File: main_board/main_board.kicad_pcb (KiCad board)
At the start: 4 copper layers, 85 x 55 mm, 45 parts, among them J1 USB_B_Micro, J2 Conn_ARM_JTAG_SWD_10, Q2 T2N7002AK,LM, U1 SSD1306, U2 ESP32-S2-SOLO, U3 TLV62568PDRLT, U4 MCP73832, Y1 SC32S-7PF20PPM

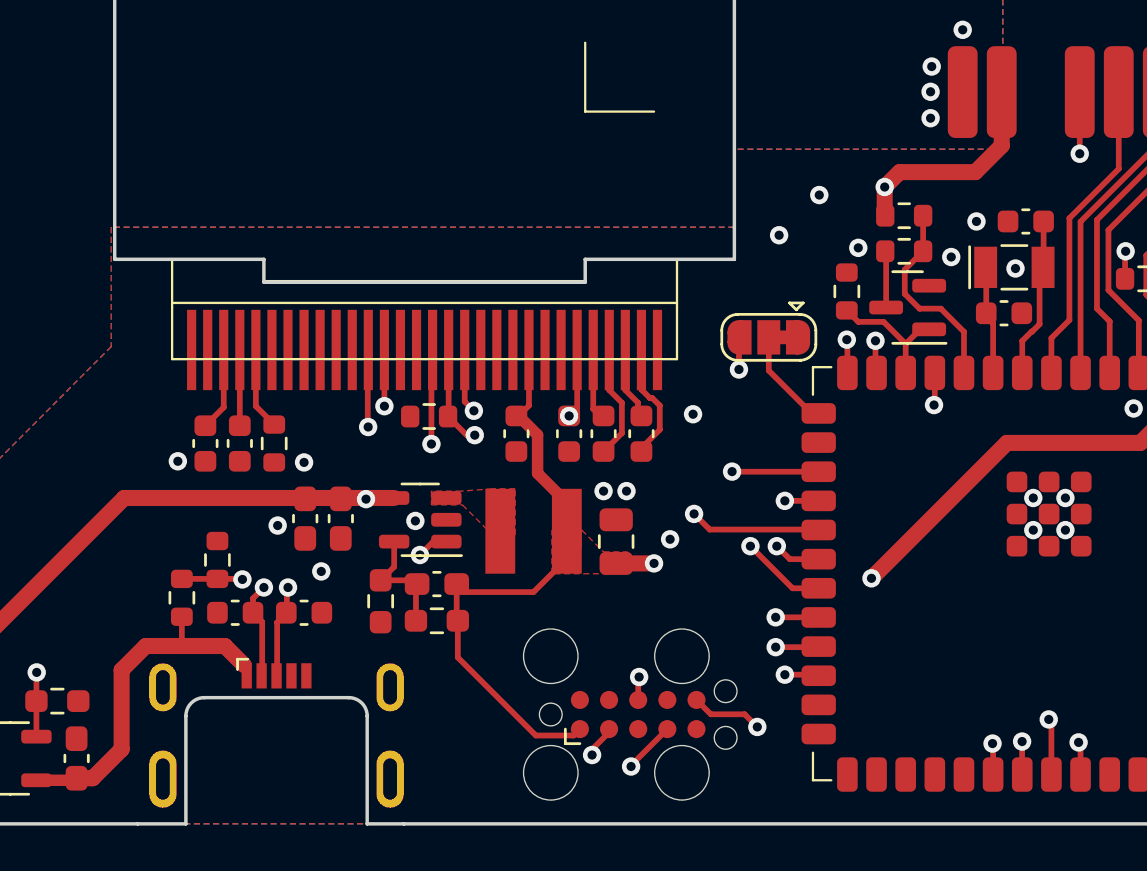
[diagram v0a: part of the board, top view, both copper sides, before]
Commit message: Fix #12: add PFET
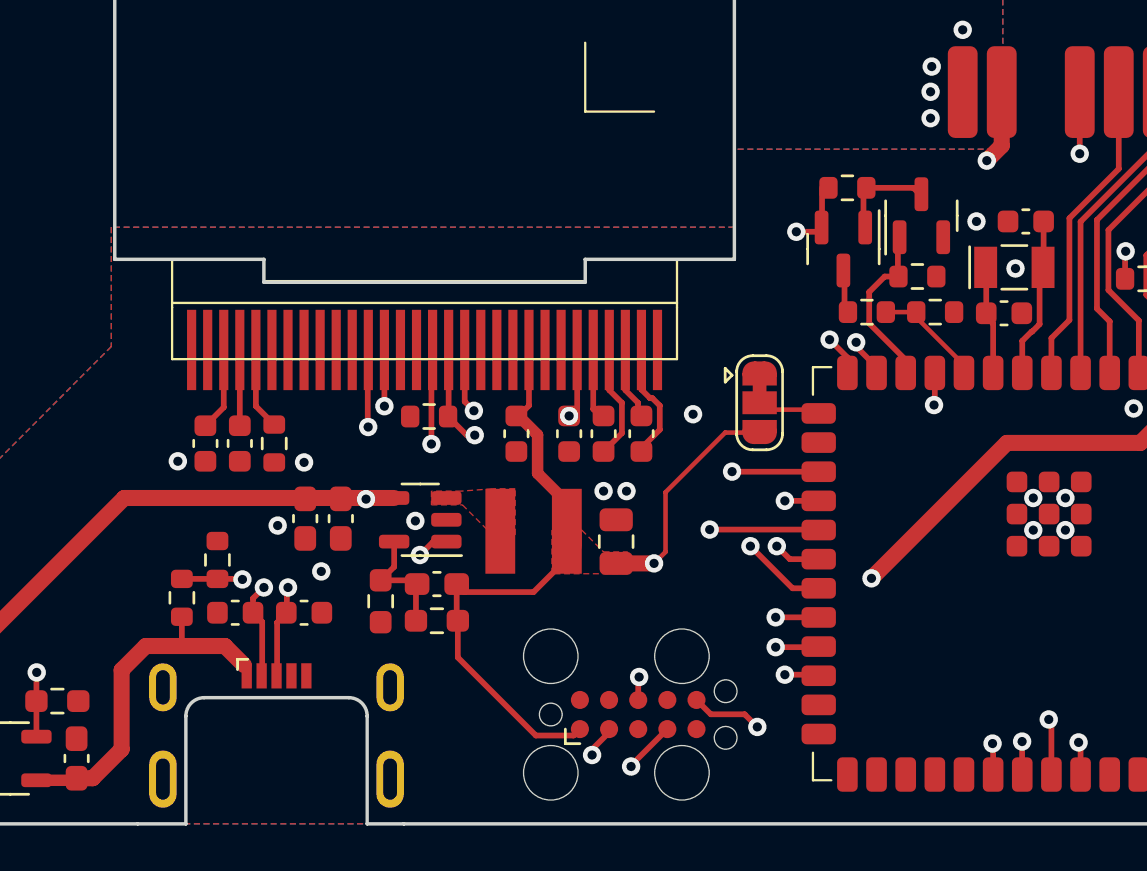
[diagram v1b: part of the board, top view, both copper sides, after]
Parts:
- added Q1: NX3008PBK,215, Package_TO_SOT_SMD:SOT-23, F.Cu at (140.8, 75.0)
- added R13: 1M, Resistor_SMD:R_0603_1608Metric, F.Cu at (140.9, 72.3)
- moved R12 4.50 mm to (141.8, 77.7)
- moved Q2 4.04 mm to (144.2, 73.5), turned to 90 degrees
- moved R9 3.14 mm to (144.0, 76.2), turned to 0 degrees
- moved R11 2.97 mm to (144.8, 77.7), turned to 0 degrees
- moved JP1 2.88 mm to (137.1, 81.7), turned to -90 degrees
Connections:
- Q2 pad 3: Net-(Q2-D) -> Net-(Q1-G)
- R11 pad 2: Net-(Q2-D) -> GND
- R12 pad 1: +BATT -> Net-(Q1-D)
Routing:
- net +3V3: track 85.4 -> 81.0 mm, vias 3 -> 2
- net Net-(Q1-G): track 0.00 -> 4.26 mm
- net /BATT_ADC: track 8.75 -> 4.84 mm
- net +BATT: track 79.9 -> 82.4 mm, vias 4 -> 5
- net Net-(Q2-D): track 2.47 -> 0.00 mm
- net Net-(Q1-D): track 0.00 -> 1.93 mm
- net /ADC_EN: track 5.72 -> 7.46 mm
- net Net-(JP1-C): track 4.40 -> 2.77 mm
- net /USB_D-: track 37.3 -> 36.7 mm
- net GND: vias 32 -> 27

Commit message: Fix #18: add RLD output, fix main board revision
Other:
- board text added: "Card/IO v1r2 Not for medical use"
- board text removed: "Card/IO v1r1 Not for medical use"
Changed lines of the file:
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@@
     (effects (font (size 1 1) (thickness 0.2) bold) (justify left bottom mirror))
   )
-  (gr_text "Card/IO v1r1\nNot for medical use" (at 129.9 53.15) (layer "B.SilkS")
+  (gr_text "Card/IO v1r2\nNot for medical use" (at 129.9 53.15) (layer "B.SilkS")
     (effects (font (size 1 1) (thickness 0.15)) (justify left bottom mirror))
   )

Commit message: Add changes to layout
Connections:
- M1 pad 10: GND -> Net-(M1-~{DRDY})
- M1 pad 11: +3V3 -> GND
- M1 pad 12: /ECG_EN -> +3V3
- M1 pad 13: /~{TOUCH} -> /ECG_CLK_EN
- M1 pad 3: GNDA -> unconnected-(M1-RLD_OUT-Pad3)
- M1 pad 4: +BATT -> GNDA
- M1 pad 5: Net-(M1-~{CS}) -> +BATT
- M1 pad 6: Net-(M1-MOSI) -> Net-(M1-~{CS})
- M1 pad 7: Net-(M1-SCLK) -> Net-(M1-MOSI)
- M1 pad 8: Net-(M1-MISO) -> Net-(M1-SCLK)
- M1 pad 9: Net-(M1-~{DRDY}) -> Net-(M1-MISO)
- U2 pad 31: unconnected-(U2-IO38-Pad31) -> /ECG_CLK_EN
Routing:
- net /ECG_CLK_EN: track 0.00 -> 51.1 mm, vias 0 -> 2
- net /ECG_EN: track 43.6 -> 46.4 mm
- net Net-(J2-NC/TDI): track 22.8 -> 23.7 mm

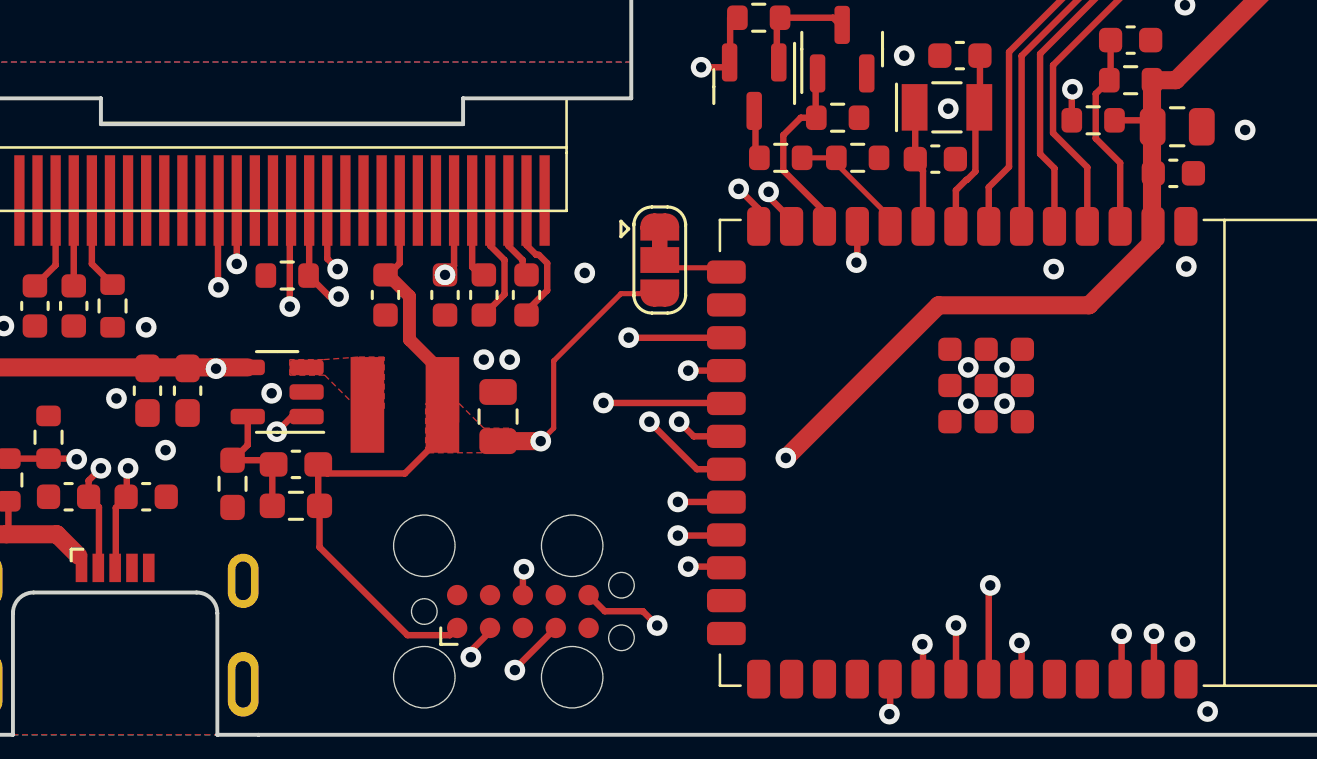
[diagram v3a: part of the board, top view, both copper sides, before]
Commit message: Fix #19: shuffle pin assignment
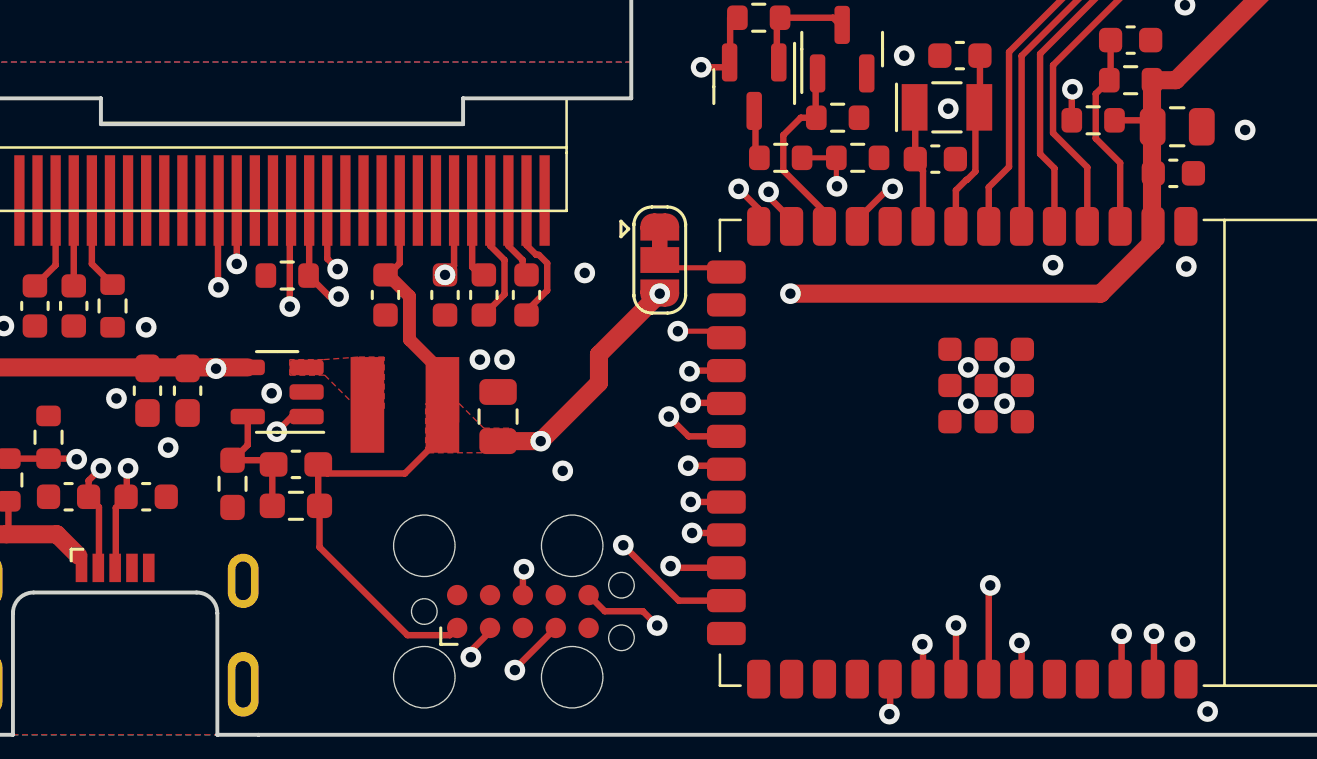
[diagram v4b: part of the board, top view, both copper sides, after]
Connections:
- U2 pad 10: /BATT_ADC -> unconnected-(U2-IO17-Pad10)
- U2 pad 17: /~{DISPLAY_RES} -> /BATT_ADC
- U2 pad 18: /~{DISPLAY_CS} -> /CHG_CURRENT
- U2 pad 19: /DISPLAY_MOSI -> /~{DISPLAY_CS}
- U2 pad 20: /DISPLAY_SCK -> /~{DISPLAY_RES}
- U2 pad 22: /CHG_CURRENT -> /DISPLAY_SCK
- U2 pad 23: /CHG_STAT -> /DISPLAY_MOSI
- U2 pad 24: /VBUS_DETECT -> /CHG_STAT
- U2 pad 25: unconnected-(U2-IO34-Pad25) -> /VBUS_DETECT
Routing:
- net +3V3: track 81.0 -> 72.6 mm, vias 2 -> 3
- net /BATT_ADC: track 4.84 -> 13.1 mm, vias 0 -> 2
- net /DISPLAY_MOSI: track 24.9 -> 27.4 mm
- net Net-(M1-~{CS}): track 21.5 -> 19.6 mm
- net /CHG_CURRENT: track 38.3 -> 40.0 mm, vias 2 -> 3
- net /DISPLAY_SCK: track 24.1 -> 25.7 mm
- net /~{DISPLAY_RES}: track 20.0 -> 21.5 mm
- net /VBUS_DETECT: track 29.9 -> 30.7 mm
- net /CHG_STAT: track 39.7 -> 40.3 mm
- net /~{DISPLAY_CS}: track 19.5 -> 20.0 mm

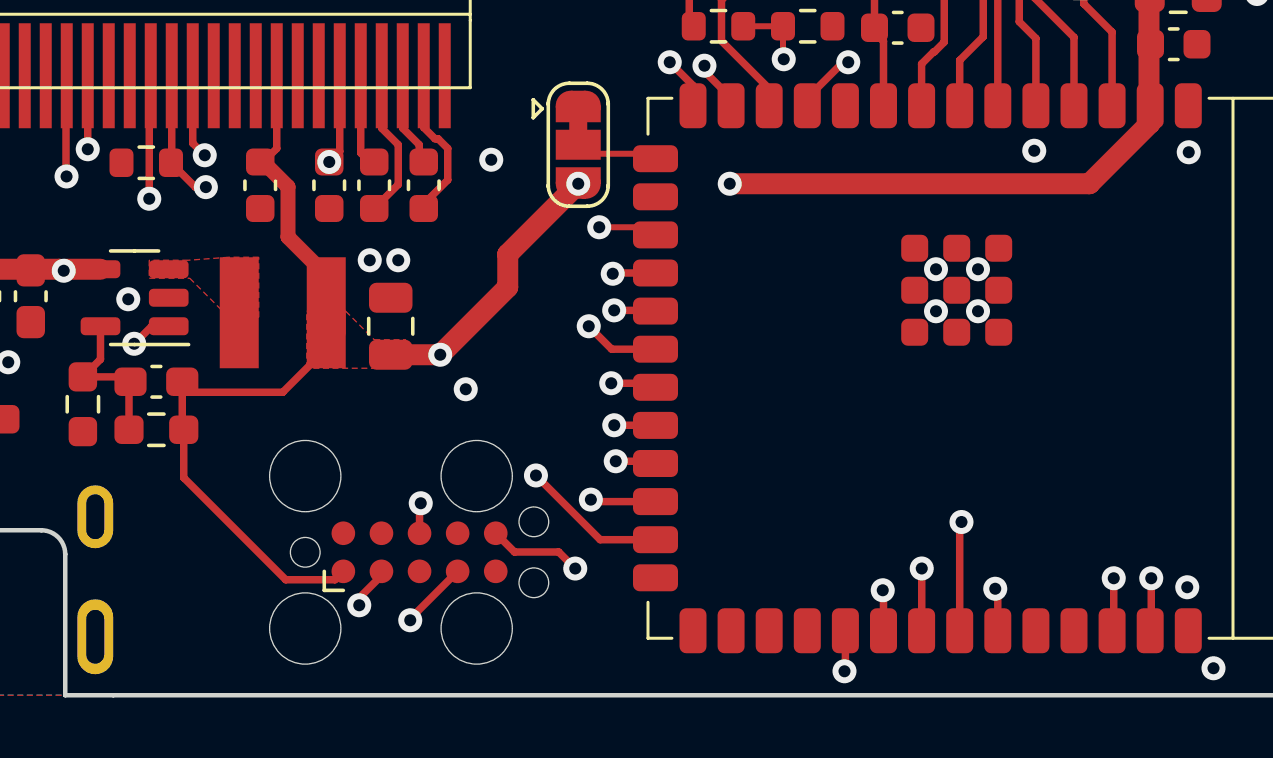
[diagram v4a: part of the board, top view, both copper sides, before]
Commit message: Fix #16: move JTAG to front side
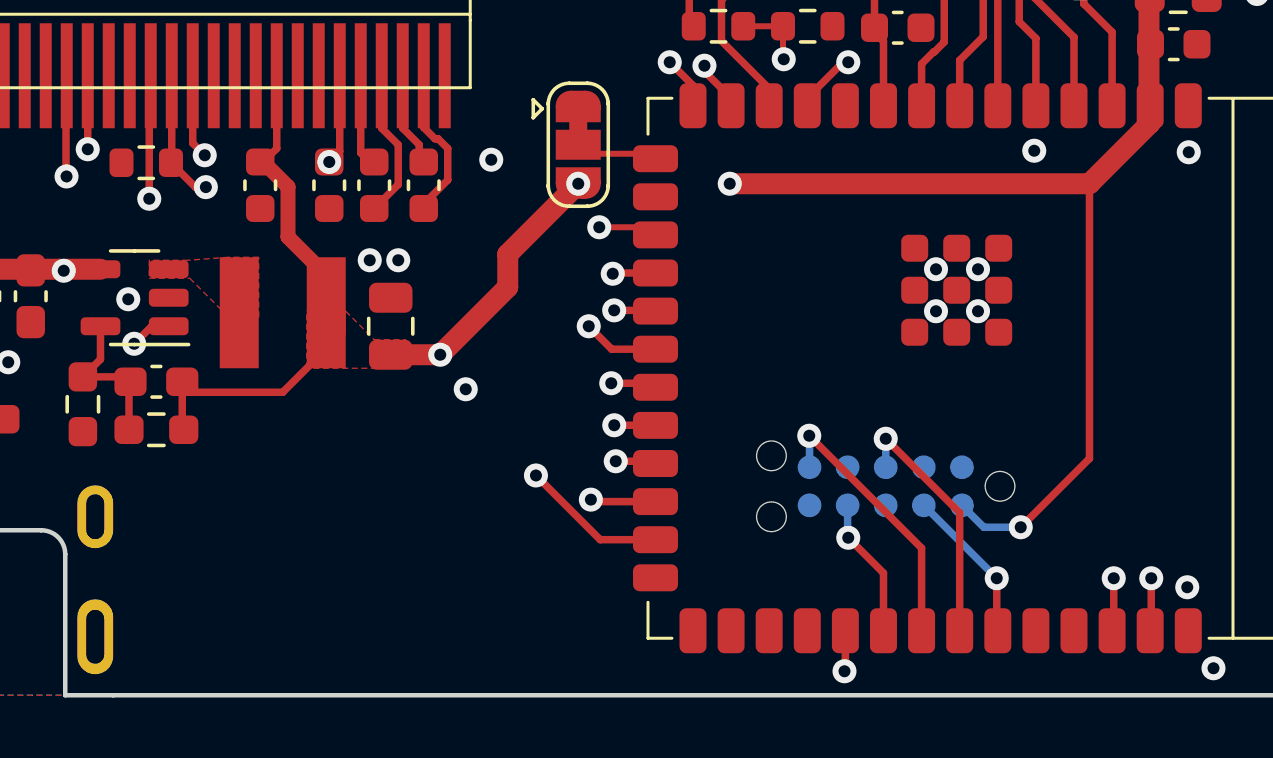
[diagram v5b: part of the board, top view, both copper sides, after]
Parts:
- J2: footprint Connector:Tag-Connect_TC2050-IDC-FP_2x05_P1.27mm_Vertical -> Connector:Tag-Connect_TC2050-IDC-NL_2x05_P1.27mm_Vertical; moved to B.Cu
- moved J2 15.7 mm to (147.3, 93.0), turned to 180 degrees
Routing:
- net Net-(J2-SWDIO/TMS): track 25.5 -> 5.20 mm, vias 2 -> 1
- net Net-(J2-SWDCLK/TCK): track 20.6 -> 4.67 mm, vias 2 -> 1
- net Net-(J2-NC/TDI): track 23.7 -> 8.37 mm, vias 2 -> 1
- net Net-(J2-SWO/TDO): track 16.8 -> 9.11 mm, vias 2 -> 1
- net +3V3: track 72.6 -> 78.8 mm, vias 3 -> 4

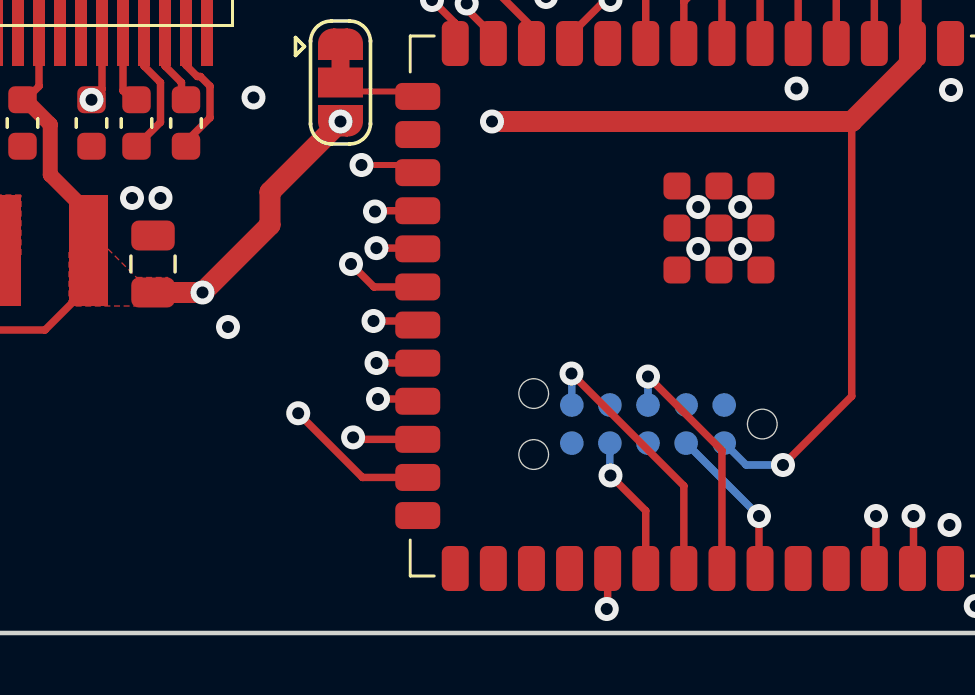
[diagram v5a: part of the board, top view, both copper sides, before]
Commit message: Tweak routing a bit
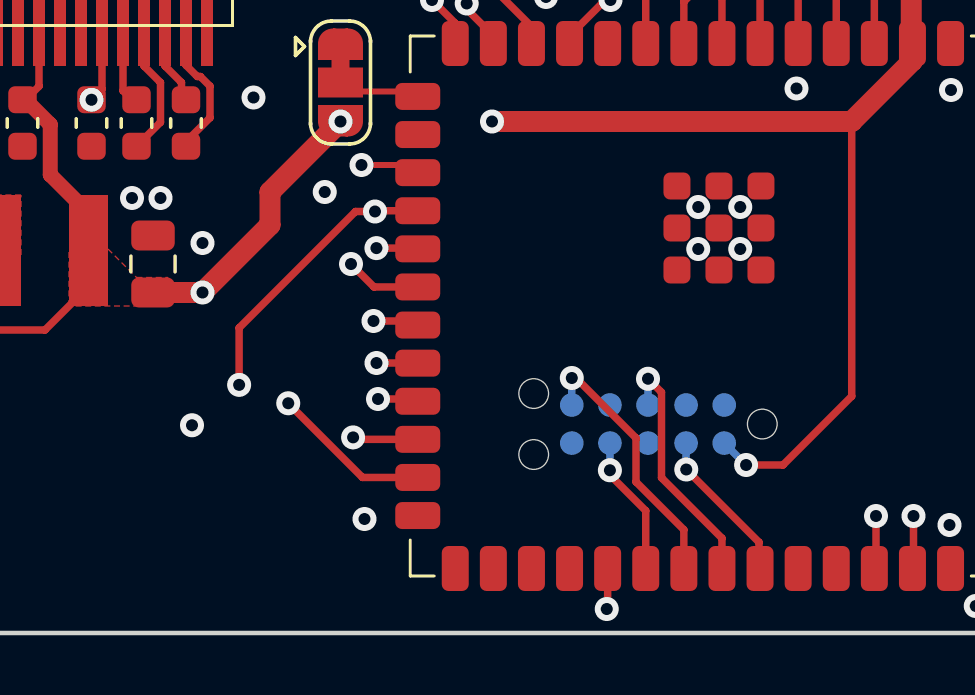
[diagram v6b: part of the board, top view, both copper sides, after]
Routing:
- net /BATT_ADC: track 13.1 -> 15.6 mm
- net /CHG_CURRENT: track 40.0 -> 41.3 mm
- net /CHG_STAT: track 40.3 -> 39.5 mm
- net GND: vias 27 -> 31
